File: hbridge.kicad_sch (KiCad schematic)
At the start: 28 parts, among them Q1 2N7000, Q11 2N7000, Q12 2N7000, Q13 2N3904, Q14 2N3906, Q15 2N3904, Q16 2N3906, Q17 STP20NF06, Q18 STP20NF06, Q2 2N7000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

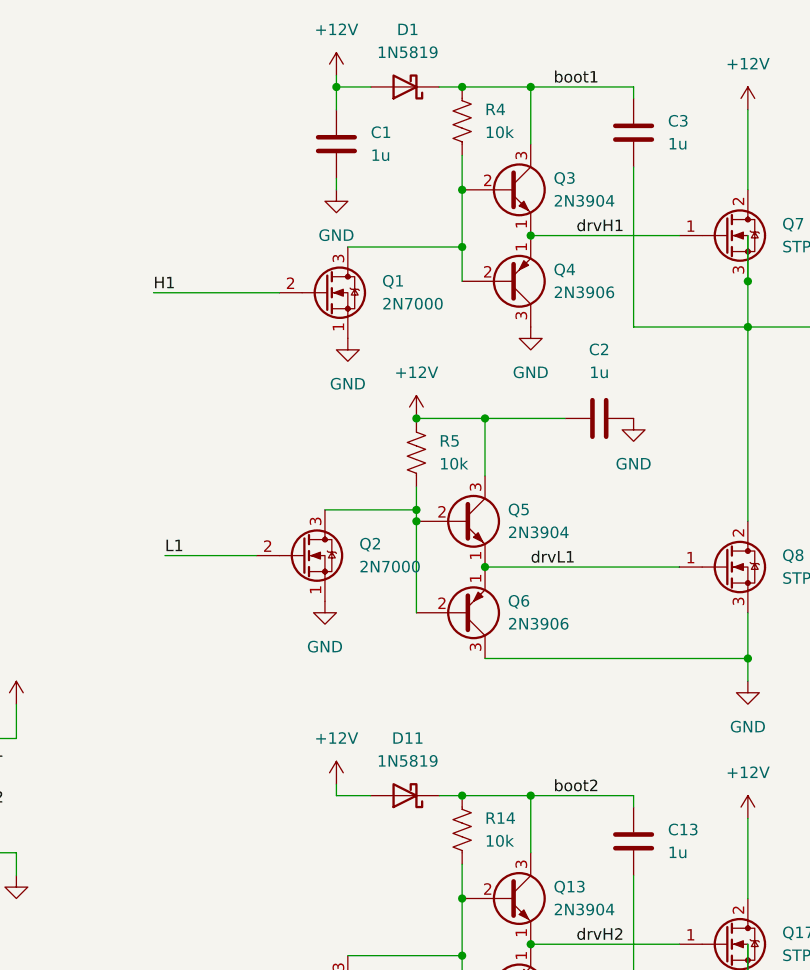
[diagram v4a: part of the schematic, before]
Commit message: Switched diodes to smd
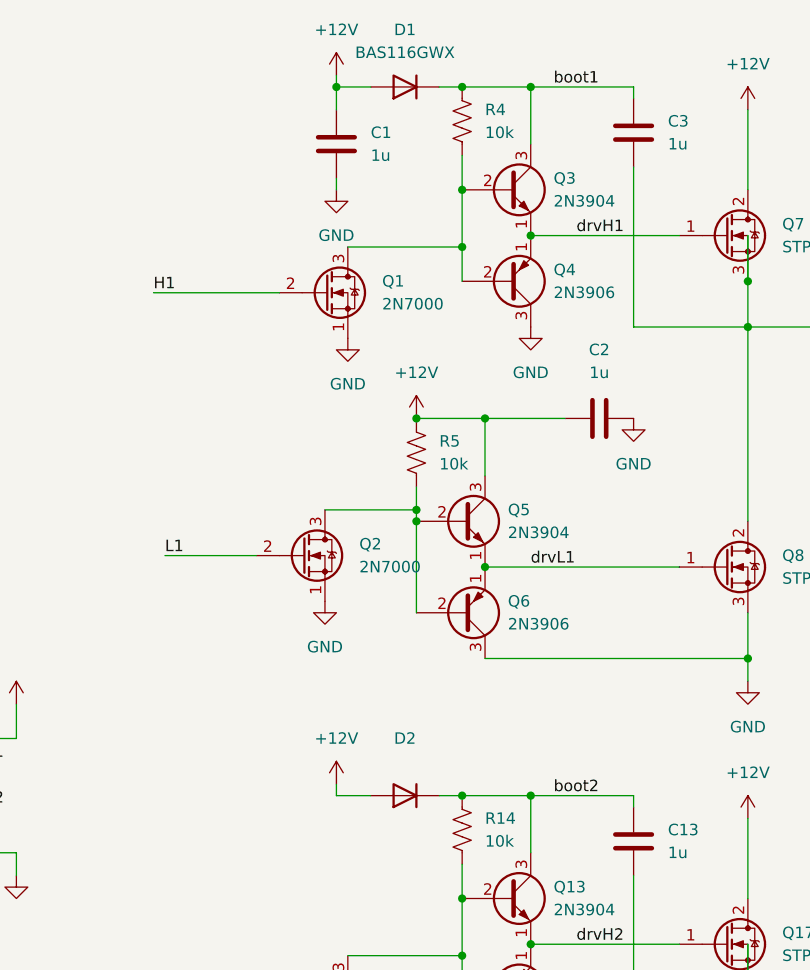
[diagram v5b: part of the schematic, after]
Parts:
- removed D1, D11: 1N5819, Diode_THT:D_DO-41_SOD81_P5.08mm_Vertical_AnodeUp, symbol Diode:1N5819
- added D1: BAS116GWX, Diode_SMD:D_SOD-123, symbol Device:D
- added D2: (no value), symbol Device:D
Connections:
- net +12V: now also D1.2 (A), D2.2 (A)
- net boot1: now also D1.1 (K)
- net boot2: now also D2.1 (K)
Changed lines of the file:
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@@
     (pin "3")
+  )
+  (symbol (lib_id "Device:D") (at 100.33 115.57 180) (unit 1)
+    (in_bom yes) (on_board yes) (fields_autoplaced)
+    (property "Reference" "D2" (id 0) (at 100.33 109.22 0))
+    (property "Value" "" (id 1) (at 100.33 111.76 0))
+    (property "Footprint" "" (id 2) (at 100.33 115.57 0)
+      (effects (font (size 1.27 1.27)) hide)
+    )
+    (property "Datasheet" "blob:https://octopart.com/3d4575ae-92c4-4db3-b58b-3a8d70e05c56" (id 3) (at 100.33 115.57 0)
+      (effects (font (size 1.27 1.27)) hide)
+    )
+    (pin "1")
+    (pin "2")
   )
   (symbol (lib_id "power:GND") (at 125.73 73.66 0) (unit 1)
@@
     (pin "3")
   )
-  (symbol (lib_id "Diode:1N5819") (at 100.33 115.57 180) (unit 1)
-    (in_bom yes) (on_board yes) (fields_autoplaced)
-    (property "Reference" "D11" (id 0) (at 100.6475 109.22 0))
-    (property "Value" "1N5819" (id 1) (at 100.6475 111.76 0))
-    (property "Footprint" "Diode_THT:D_DO-41_SOD81_P5.08mm_Vertical_AnodeUp" (id 2) (at 100.33 111.125 0)
-      (effects (font (size 1.27 1.27)) hide)
-    )
-    (property "Datasheet" "http://www.vishay.com/docs/88525/1n5817.pdf" (id 3) (at 100.33 115.57 0)
-      (effects (font (size 1.27 1.27)) hide)
-    )
-    (pin "1")
-    (pin "2")
-  )
   (symbol (lib_id "power:GND") (at 138.43 181.61 0) (unit 1)
     (in_bom yes) (on_board yes) (fields_autoplaced)
@@
     (pin "1")
   )
-  (symbol (lib_id "Diode:1N5819") (at 100.33 36.83 180) (unit 1)
-    (in_bom yes) (on_board yes) (fields_autoplaced)
-    (property "Reference" "D1" (id 0) (at 100.6475 30.48 0))
-    (property "Value" "1N5819" (id 1) (at 100.6475 33.02 0))
-    (property "Footprint" "Diode_THT:D_DO-41_SOD81_P5.08mm_Vertical_AnodeUp" (id 2) (at 100.33 32.385 0)
-      (effects (font (size 1.27 1.27)) hide)
-    )
-    (property "Datasheet" "http://www.vishay.com/docs/88525/1n5817.pdf" (id 3) (at 100.33 36.83 0)
-      (effects (font (size 1.27 1.27)) hide)
-    )
-    (pin "1")
-    (pin "2")
-  )
   (symbol (lib_id "power:+12V") (at 138.43 118.11 0) (unit 1)
     (in_bom yes) (on_board yes) (fields_autoplaced)
@@
     )
     (pin "1")
+  )
+  (symbol (lib_id "Device:D") (at 100.33 36.83 180) (unit 1)
+    (in_bom yes) (on_board yes) (fields_autoplaced)
+    (property "Reference" "D1" (id 0) (at 100.33 30.48 0))
+    (property "Value" "BAS116GWX" (id 1) (at 100.33 33.02 0))
+    (property "Footprint" "Diode_SMD:D_SOD-123" (id 2) (at 100.33 36.83 0)
+      (effects (font (size 1.27 1.27)) hide)
+    )
+    (property "Datasheet" "blob:https://octopart.com/3d4575ae-92c4-4db3-b58b-3a8d70e05c56" (id 3) (at 100.33 36.83 0)
+      (effects (font (size 1.27 1.27)) hide)
+    )
+    (pin "1")
+    (pin "2")
   )
   (symbol (lib_id "Connector:Screw_Terminal_01x04") (at 195.58 123.19 0) (unit 1)
@@
       (reference "C13") (unit 1) (value "1u") (footprint "Capacitor_SMD:C_0603_1608Metric")
     )
-    (path "/c6dd51eb-ca30-4a37-a590-4bc51f5ed94f"
-      (reference "D1") (unit 1) (value "1N5819") (footprint "Diode_THT:D_DO-41_SOD81_P5.08mm_Vertical_AnodeUp")
-    )
-    (path "/9b9cda37-3393-40e4-b7be-cdfc3a0cb753"
-      (reference "D11") (unit 1) (value "1N5819") (footprint "Diode_THT:D_DO-41_SOD81_P5.08mm_Vertical_AnodeUp")
+    (path "/edb16cfe-6d12-40e1-98de-34e7bbce167e"
+      (reference "D1") (unit 1) (value "BAS116GWX") (footprint "Diode_SMD:D_SOD-123")
+    )
+    (path "/4477d9db-925f-4112-b1a5-79d9e16e595f"
+      (reference "D2") (unit 1) (value "BAS116GWX") (footprint "Diode_SMD:D_SOD-123")
     )
     (path "/36ae561f-d236-4b22-9a73-ff22def3b3c6"

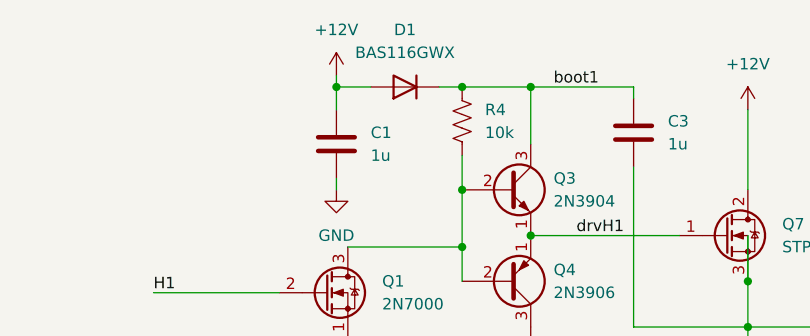
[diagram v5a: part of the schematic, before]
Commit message: Switched out diodes for more common parts
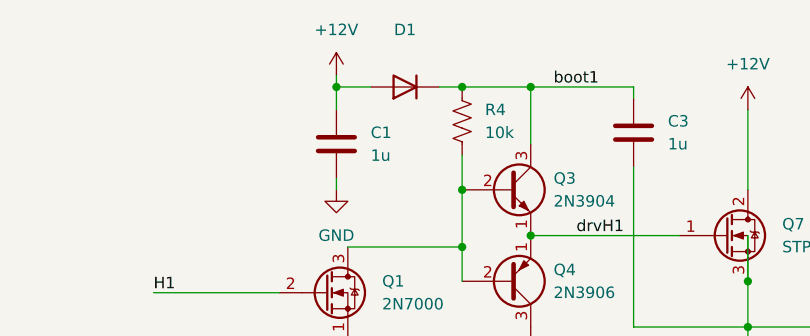
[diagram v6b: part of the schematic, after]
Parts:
- removed D1: BAS116GWX, Diode_SMD:D_SOD-123, symbol Device:D
- removed D2: (no value), symbol Device:D
- added D1, D2: (no value), symbol Diode:1N4148
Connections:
- net +12V: now also D1.2 (A), D2.2 (A)
- net boot1: now also D1.1 (K)
- net boot2: now also D2.1 (K)
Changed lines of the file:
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@@
     (pin "3")
-  )
-  (symbol (lib_id "Device:D") (at 100.33 115.57 180) (unit 1)
-    (in_bom yes) (on_board yes) (fields_autoplaced)
-    (property "Reference" "D2" (id 0) (at 100.33 109.22 0))
-    (property "Value" "" (id 1) (at 100.33 111.76 0))
-    (property "Footprint" "" (id 2) (at 100.33 115.57 0)
-      (effects (font (size 1.27 1.27)) hide)
-    )
-    (property "Datasheet" "blob:https://octopart.com/3d4575ae-92c4-4db3-b58b-3a8d70e05c56" (id 3) (at 100.33 115.57 0)
-      (effects (font (size 1.27 1.27)) hide)
-    )
-    (pin "1")
-    (pin "2")
   )
   (symbol (lib_id "power:GND") (at 125.73 73.66 0) (unit 1)
@@
     (pin "3")
   )
+  (symbol (lib_id "Diode:1N4148") (at 100.33 36.83 180) (unit 1)
+    (in_bom yes) (on_board yes) (fields_autoplaced)
+    (property "Reference" "D1" (id 0) (at 100.33 30.48 0))
+    (property "Value" "" (id 1) (at 100.33 33.02 0))
+    (property "Footprint" "" (id 2) (at 100.33 32.385 0)
+      (effects (font (size 1.27 1.27)) hide)
+    )
+    (property "Datasheet" "https://assets.nexperia.com/documents/data-sheet/1N4148_1N4448.pdf" (id 3) (at 100.33 36.83 0)
+      (effects (font (size 1.27 1.27)) hide)
+    )
+    (pin "1")
+    (pin "2")
+  )
   (symbol (lib_id "Transistor_FET:2N7000") (at 88.9 167.64 0) (unit 1)
     (in_bom yes) (on_board yes) (fields_autoplaced)
@@
     (pin "1")
   )
+  (symbol (lib_id "Diode:1N4148") (at 100.33 115.57 180) (unit 1)
+    (in_bom yes) (on_board yes) (fields_autoplaced)
+    (property "Reference" "D2" (id 0) (at 100.33 109.22 0))
+    (property "Value" "" (id 1) (at 100.33 111.76 0))
+    (property "Footprint" "" (id 2) (at 100.33 111.125 0)
+      (effects (font (size 1.27 1.27)) hide)
+    )
+    (property "Datasheet" "https://assets.nexperia.com/documents/data-sheet/1N4148_1N4448.pdf" (id 3) (at 100.33 115.57 0)
+      (effects (font (size 1.27 1.27)) hide)
+    )
+    (pin "1")
+    (pin "2")
+  )
   (symbol (lib_id "power:+12V") (at 138.43 118.11 0) (unit 1)
     (in_bom yes) (on_board yes) (fields_autoplaced)
@@
     )
     (pin "1")
-  )
-  (symbol (lib_id "Device:D") (at 100.33 36.83 180) (unit 1)
-    (in_bom yes) (on_board yes) (fields_autoplaced)
-    (property "Reference" "D1" (id 0) (at 100.33 30.48 0))
-    (property "Value" "BAS116GWX" (id 1) (at 100.33 33.02 0))
-    (property "Footprint" "Diode_SMD:D_SOD-123" (id 2) (at 100.33 36.83 0)
-      (effects (font (size 1.27 1.27)) hide)
-    )
-    (property "Datasheet" "blob:https://octopart.com/3d4575ae-92c4-4db3-b58b-3a8d70e05c56" (id 3) (at 100.33 36.83 0)
-      (effects (font (size 1.27 1.27)) hide)
-    )
-    (pin "1")
-    (pin "2")
   )
   (symbol (lib_id "Connector:Screw_Terminal_01x04") (at 195.58 123.19 0) (unit 1)
@@
       (reference "C13") (unit 1) (value "1u") (footprint "Capacitor_SMD:C_0603_1608Metric")
     )
-    (path "/edb16cfe-6d12-40e1-98de-34e7bbce167e"
-      (reference "D1") (unit 1) (value "BAS116GWX") (footprint "Diode_SMD:D_SOD-123")
-    )
-    (path "/4477d9db-925f-4112-b1a5-79d9e16e595f"
-      (reference "D2") (unit 1) (value "BAS116GWX") (footprint "Diode_SMD:D_SOD-123")
+    (path "/85750ffe-db8b-44b0-b700-bcbc8d7aeacf"
+      (reference "D1") (unit 1) (value "1N4148") (footprint "Diode_THT:D_DO-35_SOD27_P7.62mm_Horizontal")
+    )
+    (path "/c6d633ac-10cd-4582-928c-6ccb80a48749"
+      (reference "D2") (unit 1) (value "1N4148") (footprint "Diode_THT:D_DO-35_SOD27_P7.62mm_Horizontal")
     )
     (path "/36ae561f-d236-4b22-9a73-ff22def3b3c6"

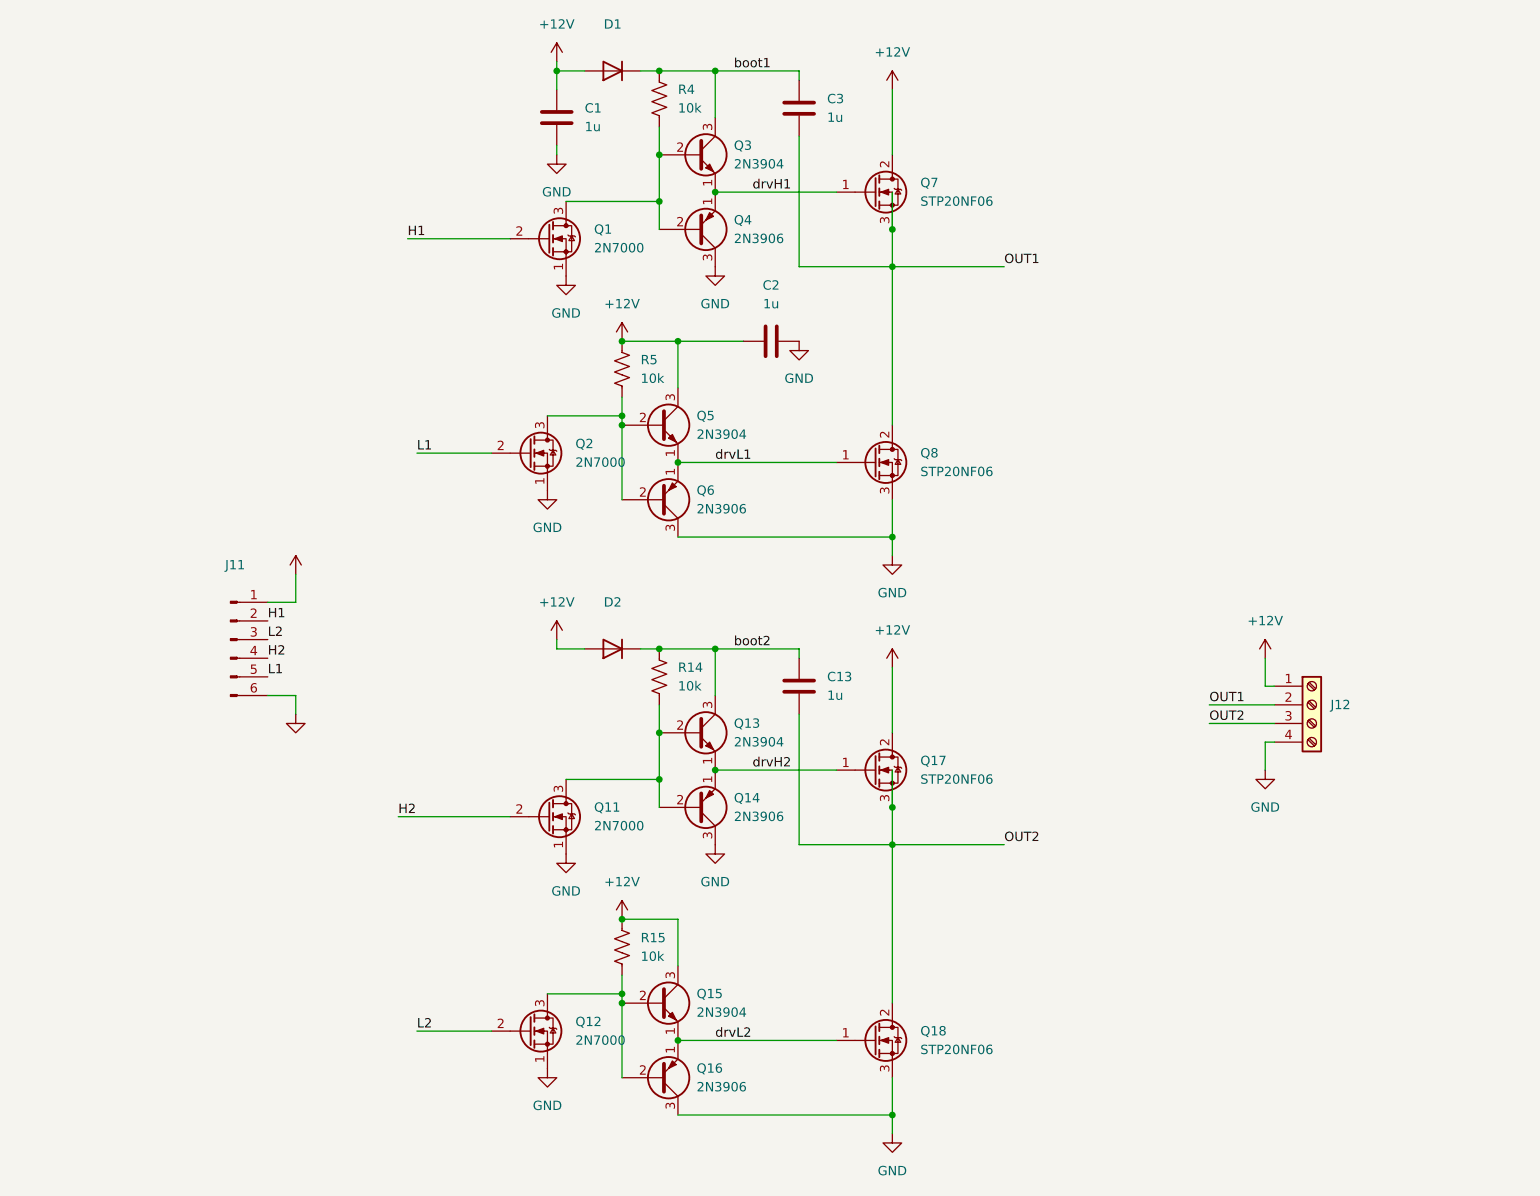
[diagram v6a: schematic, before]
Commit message: Added logic to simplify control
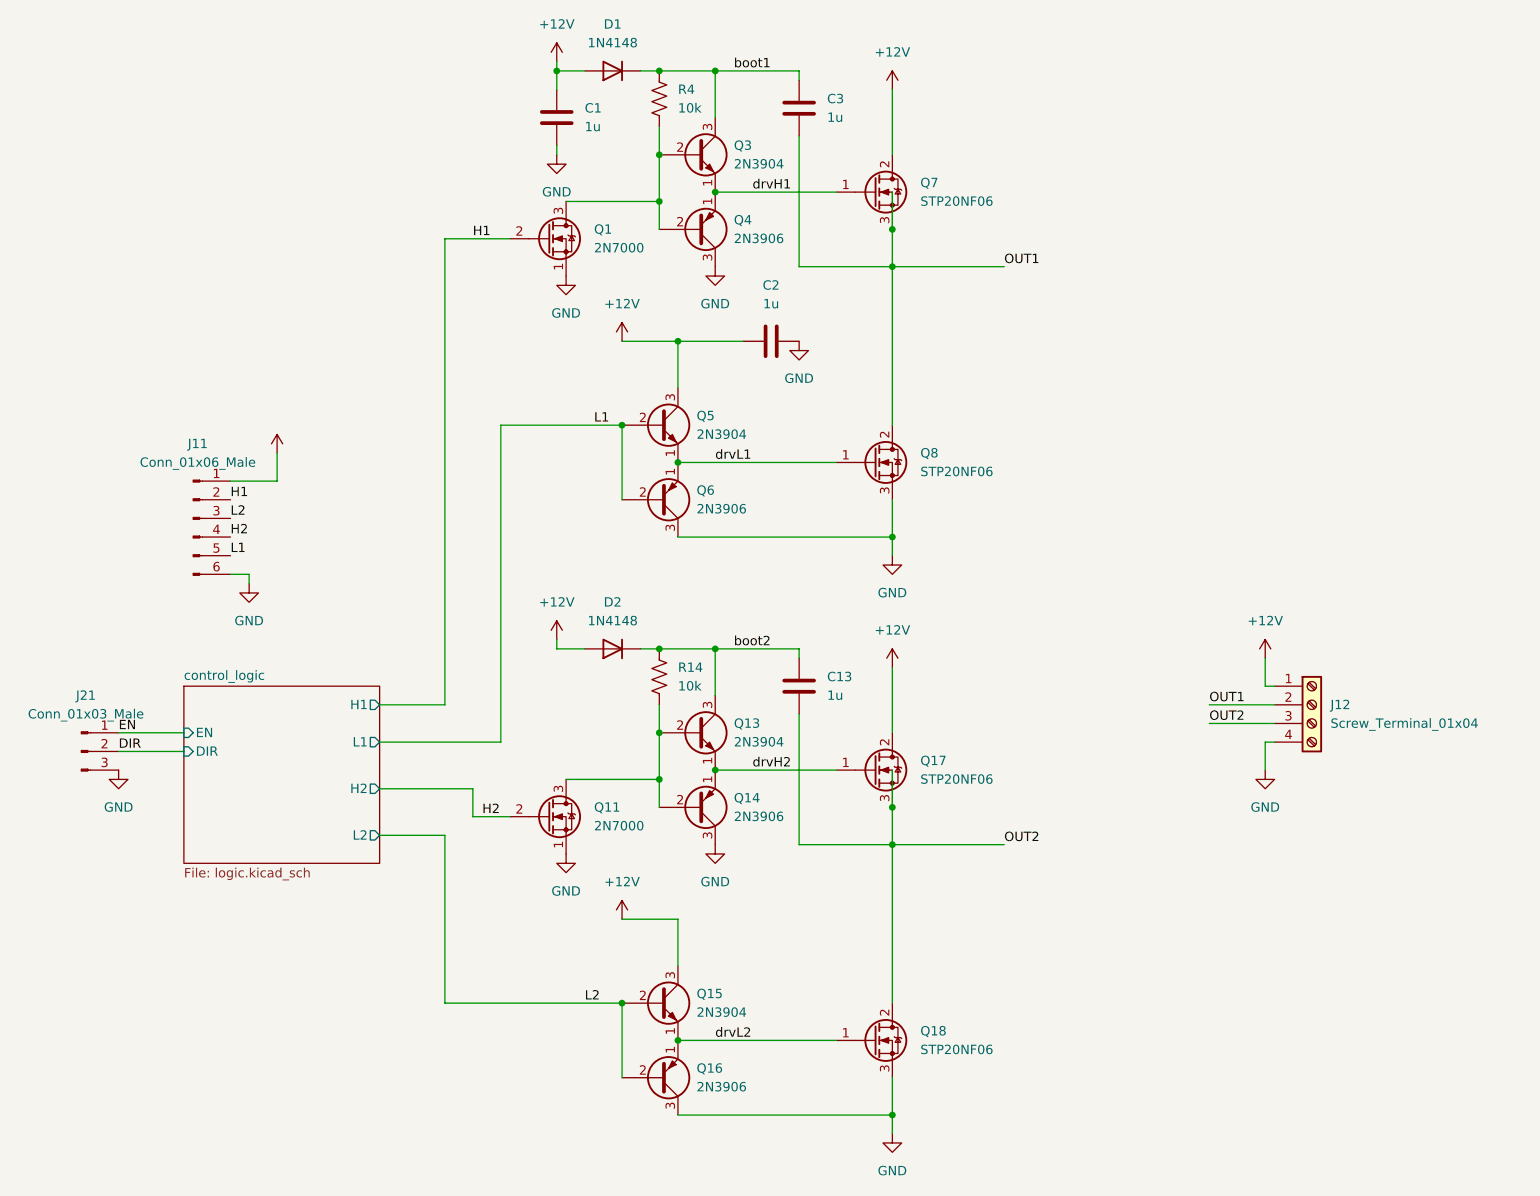
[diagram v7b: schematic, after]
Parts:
- removed Q12, Q2: 2N7000, Package_TO_SOT_THT:TO-92_Inline, symbol Transistor_FET:2N7000
- removed R15, R5: 10k, symbol Device:R_US
- added J21: Conn_01x03_Male, Connector_PinHeader_2.54mm:PinHeader_1x03_P2.54mm_Vertical, symbol Connector:Conn_01x03_Male
- C1, C13, C2, C3: footprint (none) -> Capacitor_SMD:C_0603_1608Metric
- D1, D2: value (none) -> 1N4148; footprint (none) -> Diode_THT:D_DO-35_SOD27_P7.62mm_Horizontal
- J11: value (none) -> Conn_01x06_Male; footprint (none) -> Connector_PinHeader_2.54mm:PinHeader_1x06_P2.54mm_Vertical
- J12: value (none) -> Screw_Terminal_01x04; footprint (none) -> Connector_Phoenix_MSTB:PhoenixContact_MSTBVA_2,5_4-G_1x04_P5.00mm_Vertical
- R14, R4: footprint (none) -> Resistor_SMD:R_0603_1608Metric
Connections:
- net +5V is gone; now on net +12V: J11.1 (Pin_1)
- net GND: now also J21.3 (Pin_3)
- net L1: now also Q5.2 (B), Q6.2 (B)
- net L2: now also Q15.2 (B), Q16.2 (B)
- new net DIR: J21.2 (Pin_2)
- new net EN: J21.1 (Pin_1)
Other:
- added sheet control_logic (logic.kicad_sch)
